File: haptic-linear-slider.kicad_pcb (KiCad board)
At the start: 2 copper layers, 130.5 x 33.8 mm, 79 parts, among them IC1 DIO54335TST6, IC2 TLV61048DBVR, J1 SWD, J2 USB_C_Receptacle_USB2.0_16P, J3 TBC05-02-1-G-G, J4 EXT_CTRL, SW1 SW_Reset, SW2 SW_Boot, U1 RP2354A, U2 PSM01-081A-103B2, U3 DRV8876PWPR, U4 USBLC6-2SC6, Y1 ABM8-272-T3

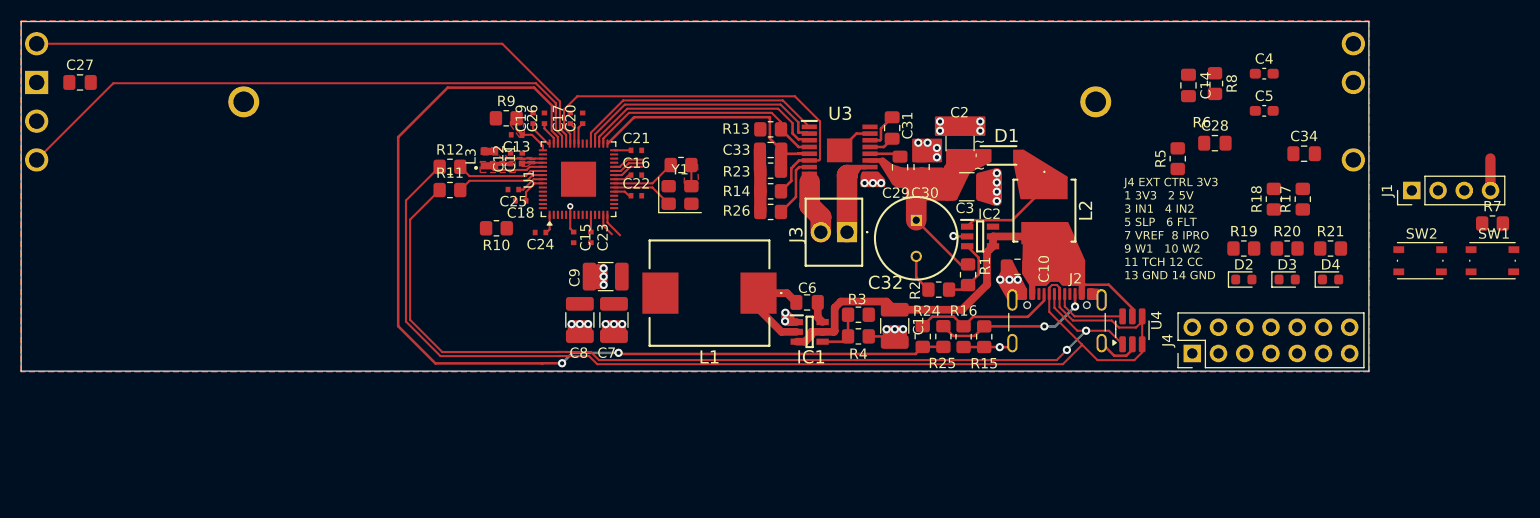
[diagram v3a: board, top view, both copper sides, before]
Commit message: nuovo micro e altro IC che si saldano meglio, routing rifatto ma va ancora rivisto
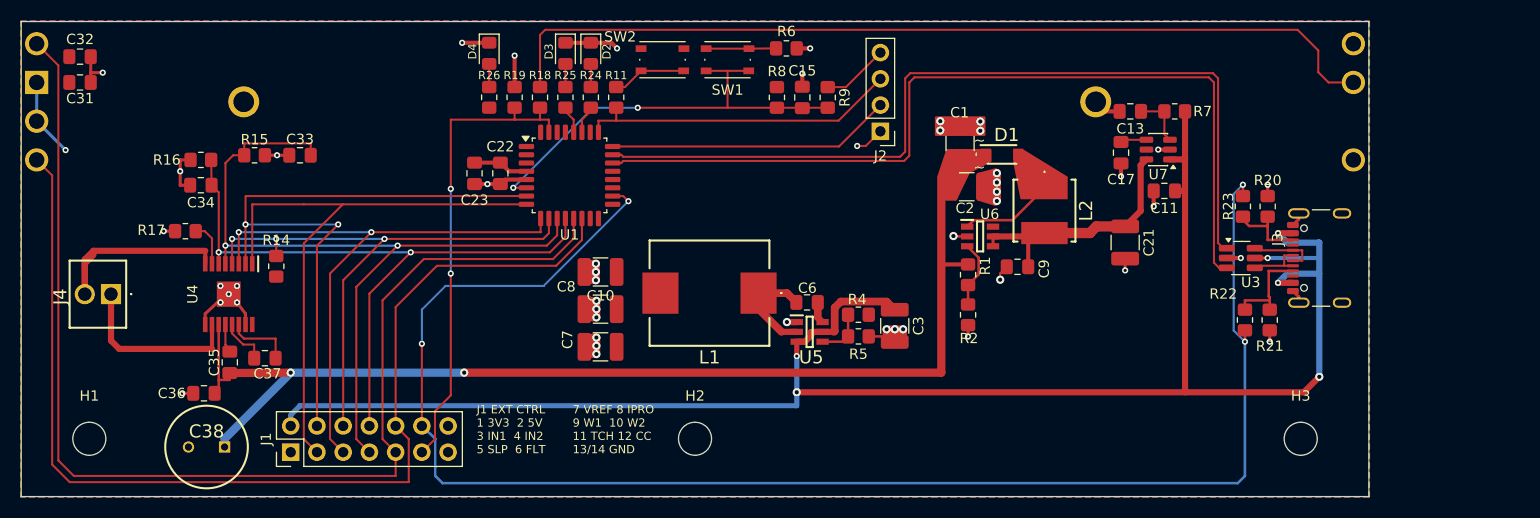
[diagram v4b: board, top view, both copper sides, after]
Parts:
- removed C12: 4u7, _Footprints:C_0402_1005Metric_small_pads
- removed the C15 at (263.4, 220.5)
- removed C16, C20, C24, C25, C26: 100n, _Footprints:C_0402_1005Metric_small_pads
- removed the C22 at (269.5, 216.5)
- removed the C23 at (265.1, 220.5)
- removed C4, C5: 15p, Capacitor_SMD:C_0603_1608Metric_Pad1.08x0.95mm_HandSolder
- removed the C9 at (266.5, 224.3)
- removed L3: 3u3, _Footprints:L_pol_2016
- removed the R11 at (251.4, 215.9)
- removed R12: 27, Resistor_SMD:R_0805_2012Metric_Pad1.20x1.40mm_HandSolder
- removed the R6 at (273.8, 213.5)
- removed the R9 at (256.9, 209.0)
- removed Y1: ABM8-272-T3, _Footprints:ABM8-272-T3
- added C10: 10u, Capacitor_SMD:C_1210_3225Metric_Pad1.33x2.70mm_HandSolder, F.Cu at (266.0, 223.8)
- added H1: MountingHole, MountingHole:MountingHole_3.2mm_M3, F.Cu at (216.5, 240.0)
- added H2: MountingHole, MountingHole:MountingHole_3.2mm_M3, F.Cu at (275.1, 240.0)
- added H3: MountingHole, MountingHole:MountingHole_3.2mm_M3, F.Cu at (333.8, 240.0)
- added R7: 100k, Resistor_SMD:R_0805_2012Metric_Pad1.20x1.40mm_HandSolder, F.Cu at (321.6, 208.3)
- added U7: TPS22918DBVR, Package_TO_SOT_SMD:SOT-23-6, F.Cu at (320.0, 212.0)
- C11, C13: value 4u7 -> 1u; footprint _Footprints:C_0402_1005Metric_small_pads -> Capacitor_SMD:C_0805_2012Metric_Pad1.18x1.45mm_HandSolder
- C17: value 100n -> 3n3; footprint _Footprints:C_0402_1005Metric_small_pads -> Capacitor_SMD:C_0805_2012Metric_Pad1.18x1.45mm_HandSolder
- C21: value 100n -> 47u; footprint _Footprints:C_0402_1005Metric_small_pads -> Capacitor_SMD:C_1210_3225Metric_Pad1.33x2.70mm_HandSolder
- C22: renamed from C18; footprint _Footprints:C_0402_1005Metric_small_pads -> Capacitor_SMD:C_0805_2012Metric_Pad1.18x1.45mm_HandSolder
- C23: renamed from C19; value 100n -> 4u7; footprint _Footprints:C_0402_1005Metric_small_pads -> Capacitor_SMD:C_0805_2012Metric_Pad1.18x1.45mm_HandSolder
- D2, D3, D4: footprint LED_SMD:LED_0603_1608Metric -> LED_SMD:LED_0805_2012Metric_Pad1.15x1.40mm_HandSolder
- U1: value RP2354A -> STM32C071KBT6; footprint _Footprints:RP2354A_QFN-60-1EP_7x7mm_P0.4mm_EP3.4x3.4mm -> Package_QFP:LQFP-32_7x7mm_P0.8mm
- moved C32 110.2 mm to (215.6, 203.0)
- moved C34 106.9 mm to (227.3, 215.4), turned to 180 degrees
- moved J1 87.8 mm to (236.0, 241.3)
- moved D4 84.4 mm to (255.2, 202.7), turned to -90 degrees
- moved R26 82.8 mm to (255.2, 206.9), turned to 90 degrees
- moved SW1 76.6 mm to (278.3, 203.3)
- moved SW2 75.9 mm to (272.0, 203.3)
- moved R18 74.5 mm to (260.1, 206.9), turned to -90 degrees
- moved R19 74.2 mm to (257.7, 206.9)
- moved D3 73.2 mm to (262.6, 202.7), turned to -90 degrees
- moved C36 72.9 mm to (227.6, 235.6), turned to 180 degrees
- moved J4 71.5 mm to (218.6, 226.0)
- moved R25 71.4 mm to (262.6, 206.9), turned to 90 degrees
- moved C38 70.5 mm to (229.6, 240.8), turned to 180 degrees
- moved R6 70.4 mm to (284.0, 202.2)
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- renumbered C2 to C1, C14 to C15, C3 to C2, C1 to C3, C27 to C31, C28 to C32, C29 to C35, C30 to C36, C31 to C37, C32 to C38, C10 to C9, J4 to J1, J1 to J2, J2 to J3, J3 to J4, R10 to R11, R13 to R14, R23 to R15, R14 to R16, R26 to R17, R17 to R18, R18 to R19, R15 to R20, R16 to R21, R24 to R22, R25 to R23, R19 to R24, R20 to R25, R21 to R26, R3 to R4, R4 to R5, R7 to R6, R5 to R9, U4 to U3, U3 to U4, IC1 to U5, IC2 to U6
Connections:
- net /CC1 renamed Net-(J3-CC1)
- net /CC2 renamed Net-(J3-CC2)
- net /~{USB_BOOT} renamed /BOOT0
- net Net-(D1-A) renamed /BOOST_SW
- net Net-(IC1-SW) renamed /BUCK_SW
- net Net-(U3-OUT1) renamed /MOTOR_OUT1
- net Net-(U3-OUT2) renamed /MOTOR_OUT2
- C11 pad 1: +3V3 -> +5V
- C13 pad 1: Net-(U1-VREG_AVDD) -> /LS_ON
- C15 pad 2: /RUN -> /NRST
- C17 pad 1: +1V1 -> /LS_CT
- C21 pad 1: +3V3 -> /+5V_MOT
- C9 pad 1: +5V -> /+5V_MOT
- J2 pad 2: /SWCLK -> /SWD
- J2 pad 3: /SWD -> /SWCLK
- J3 pad A6: /USB_D+ -> Net-(J3-D+-PadA6)
- J3 pad A7: /USB_D- -> Net-(J3-D--PadA7)
- J3 pad B6: /USB_D+ -> Net-(J3-D+-PadA6)
- J3 pad B7: /USB_D- -> Net-(J3-D--PadA7)
- L2 pad 2: +5V -> /+5V_MOT
- R11 pad 1: Net-(U1-QSPI_SS) -> /SWCLK
- R8 pad 2: /RUN -> /NRST
- R9 pad 2: /RUN -> /NRST
- SW1 pad 2: /RUN -> /NRST
- SW2 pad 1: GND -> +3V3
- U1 pad 1: +3V3 -> unconnected-(U1-PB9-Pad1)
- U1 pad 10: unconnected-(U1-GPIO7-Pad10) -> /MOTOR_~{FAULT}
- U1 pad 11: +3V3 -> /MOTOR_VREF_PWM
- U1 pad 12: unconnected-(U1-GPIO8-Pad12) -> /MOTOR_IPROPI
- U1 pad 13: unconnected-(U1-GPIO9-Pad13) -> /POT_WIPER1
- U1 pad 14: /STATUS_LED1 -> /POT_WIPER2
- U1 pad 15: /STATUS_LED2 -> unconnected-(U1-PB0-Pad15)
- U1 pad 18: unconnected-(U1-GPIO14-Pad18) -> /CC_SENSE
- U1 pad 20: +3V3 -> unconnected-(U1-PC6-Pad20)
- U1 pad 21: /XIN -> unconnected-(U1-PA10-Pad21)
- U1 pad 22: /XOUT -> /USB_D-
- U1 pad 23: +1V1 -> /USB_D+
- U1 pad 24: /SWCLK -> /SWD
- U1 pad 25: /SWD -> /SWCLK
- U1 pad 26: /RUN -> unconnected-(U1-PA15-Pad26)
- U1 pad 27: unconnected-(U1-GPIO16-Pad27) -> /STATUS_LED1
- U1 pad 28: unconnected-(U1-GPIO17-Pad28) -> /STATUS_LED2
- U1 pad 30: +3V3 -> unconnected-(U1-PB6-Pad30)
- U1 pad 31: /MOTOR_VREF_PWM -> /TOUCH_SENSE
- U1 pad 32: /MOTOR_~{FAULT} -> unconnected-(U1-PB8-Pad32)
- U1 pad 4: unconnected-(U1-GPIO2-Pad4) -> +3V3
- U1 pad 5: unconnected-(U1-GPIO3-Pad5) -> GND
- U1 pad 6: +1V1 -> /NRST
- U1 pad 7: unconnected-(U1-GPIO4-Pad7) -> /MOTOR_IN2
- U1 pad 8: unconnected-(U1-GPIO5-Pad8) -> /MOTOR_IN1
- U1 pad 9: unconnected-(U1-GPIO6-Pad9) -> /MOTOR_~{SLEEP}
- U3 pad 4: /USB_D- -> Net-(J3-D--PadA7)
- U3 pad 6: /USB_D+ -> Net-(J3-D+-PadA6)
- U6 pad 4: +5V -> /+5V_MOT
- U6 pad 5: +5V -> /+5V_MOT
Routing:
- net +5V: track 42.3 -> 181.3 mm, vias 0 -> 6
- net +10V: track 23.5 -> 111.0 mm, vias 0 -> 2
- net Net-(U2-T): track 0.00 -> 87.3 mm
- net /CC_SENSE: track 94.9 -> 152.9 mm, vias 2 -> 4
- net /POT_WIPER1: track 57.3 -> 114.9 mm
- net /MOTOR_VREF_PWM: track 26.4 -> 77.0 mm, vias 0 -> 2
- net /POT_WIPER2: track 59.1 -> 105.6 mm
- net /TOUCH_SENSE: track 0.00 -> 46.4 mm, vias 0 -> 2
- net /NRST: track 0.00 -> 42.6 mm, vias 0 -> 2
- net /MOTOR_IN2: track 24.6 -> 63.2 mm, vias 0 -> 2
- net /MOTOR_IN1: track 24.6 -> 58.4 mm
- net /MOTOR_~{SLEEP}: track 24.0 -> 57.1 mm, vias 0 -> 2
- net /MOTOR_~{FAULT}: track 24.0 -> 56.2 mm, vias 0 -> 3
- net /USB_D-: track 114.8 -> 84.9 mm
- net /SWCLK: track 3.08 -> 31.4 mm
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- removed copper zone on F.Cu, net +1V1
- removed copper zone on F.Cu, net Net-(C5-Pad1)
- removed copper zone on F.Cu, net Net-(U1-VREG_AVDD)
- removed copper zone on F.Cu, net Net-(U1-VREG_LX)
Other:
- board size 130.5 x 33.8 mm -> 130.5 x 46 mm
- board text added: "7 VREF 8 IPRO 9 W1 10 W2 11 TCH 12 CC 13/14 GND"
- board text added: "J1 EXT CTRL 1 3V3 2 5V 3 IN1 4 IN2 5 SLP 6 FLT"
- board text removed: "J4 EXT CTRL 3V3 1 3V3 2 5V 3 IN1 4 IN2 5 SLP 6 FLT 7 VREF 8 IPRO 9 W1 10 W2 11 TCH 12 CC 13 GND 14 GND"

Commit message: spostato J2
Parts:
- moved J2 10.5 mm to (287.2, 219.0), turned to 90 degrees
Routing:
- net Net-(J2-Pin_4): track 6.48 -> 17.0 mm, vias 0 -> 1
- net /SWCLK: track 31.4 -> 36.8 mm, vias 0 -> 1
- net GND: track 84.9 -> 82.0 mm, vias 48 -> 47
- net /SWD: track 27.6 -> 28.9 mm, vias 0 -> 1
